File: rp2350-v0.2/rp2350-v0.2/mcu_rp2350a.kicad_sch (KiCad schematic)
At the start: 33 parts, among them SW4 RUN, SW5 BOOTSEL, U1 RP2350A-QFN60, Y1 ABM8-272-T3, Y2 SIT1533AI-H4-DCC-32.768E

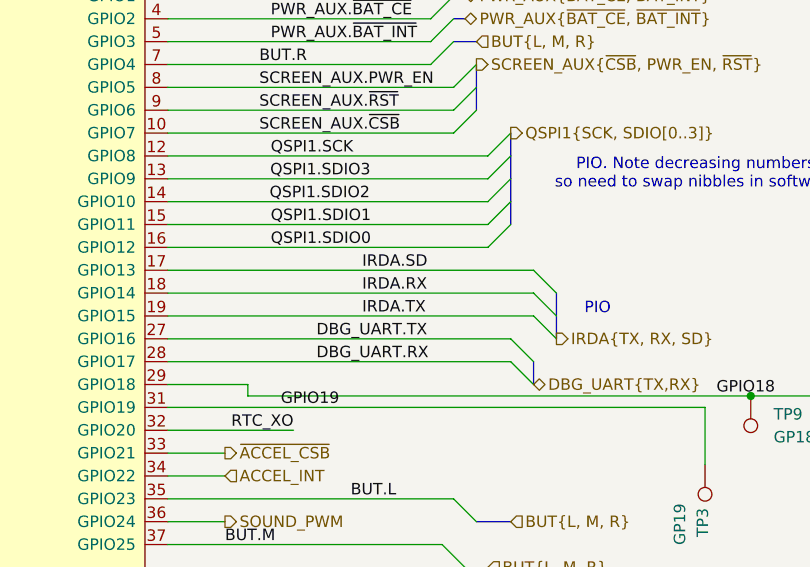
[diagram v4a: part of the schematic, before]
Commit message: v0.2: final big checks done, fixed IrDA footprint
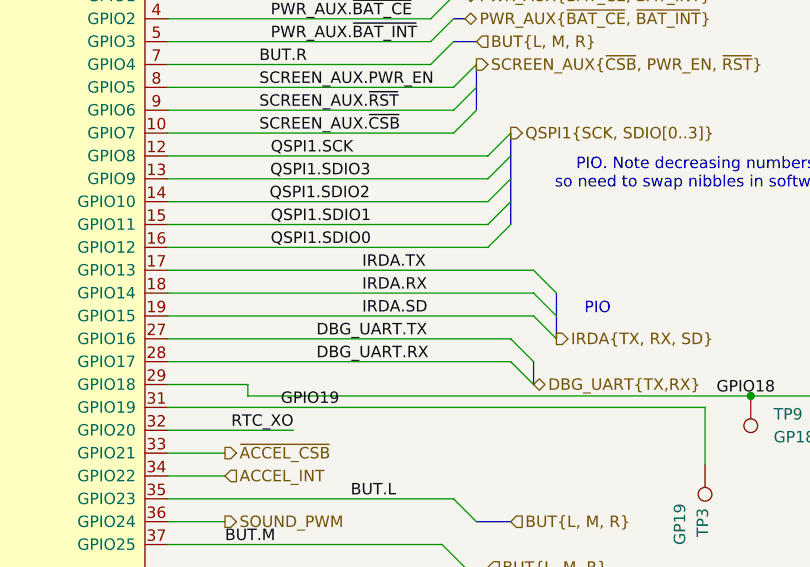
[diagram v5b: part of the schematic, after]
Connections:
- net IRDA.SD: now also U1.19 (GPIO15); no longer U1.17 (GPIO13)
- net IRDA.TX: now also U1.17 (GPIO13); no longer U1.19 (GPIO15)
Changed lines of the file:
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@@
 		)
 	)
-	(label "IRDA.TX"
+	(label "IRDA.SD"
 		(at 224.79 83.82 0)
 		(effects
@@
 		)
 	)
-	(label "IRDA.SD"
+	(label "IRDA.TX"
 		(at 224.79 78.74 0)
 		(effects

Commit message: v0.2: sent to jlc
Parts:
- added R24, R25: 10k, Resistor_SMD:R_0402_1005Metric, symbol Device:R
- R29: value R -> 1k
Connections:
- net +3.3V: now also R24.1, R25.1
- net I2C.SCL: now also R25.2
- net I2C.SDA: now also R24.2
